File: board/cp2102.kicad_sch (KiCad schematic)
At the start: 7 parts, among them U1 CP2102N-Axx-xQFN28

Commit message: finished layout
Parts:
- C1, C2: footprint (none) -> Capacitor_SMD:C_0603_1608Metric
- R1, R2, R3, R6: footprint (none) -> Resistor_SMD:R_0603_1608Metric
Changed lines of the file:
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@@
       (effects (font (size 1.27 1.27)) (justify left))
     )
-    (property "Footprint" "" (at 125.73 86.36 0)
+    (property "Footprint" "Capacitor_SMD:C_0603_1608Metric" (at 125.73 86.36 0)
       (effects (font (size 1.27 1.27)) hide)
     )
@@
       (effects (font (size 1.27 1.27)) (justify left))
     )
-    (property "Footprint" "" (at 139.7 60.325 0)
+    (property "Footprint" "Resistor_SMD:R_0603_1608Metric" (at 139.7 60.325 0)
       (effects (font (size 1.27 1.27)) hide)
     )
@@
       (effects (font (size 1.27 1.27)))
     )
-    (property "Footprint" "" (at 175.26 94.615 0)
+    (property "Footprint" "Resistor_SMD:R_0603_1608Metric" (at 175.26 94.615 0)
       (effects (font (size 1.27 1.27)) hide)
     )
@@
       (effects (font (size 1.27 1.27)) (justify left))
     )
-    (property "Footprint" "" (at 163.83 57.785 0)
+    (property "Footprint" "Capacitor_SMD:C_0603_1608Metric" (at 163.83 57.785 0)
       (effects (font (size 1.27 1.27)) hide)
     )
@@
       (effects (font (size 1.27 1.27)) (justify left))
     )
-    (property "Footprint" "" (at 116.205 77.47 0)
+    (property "Footprint" "Resistor_SMD:R_0603_1608Metric" (at 116.205 77.47 0)
       (effects (font (size 1.27 1.27)) hide)
     )
@@
       (effects (font (size 1.27 1.27)) (justify left))
     )
-    (property "Footprint" "" (at 116.205 86.36 0)
+    (property "Footprint" "Resistor_SMD:R_0603_1608Metric" (at 116.205 86.36 0)
       (effects (font (size 1.27 1.27)) hide)
     )

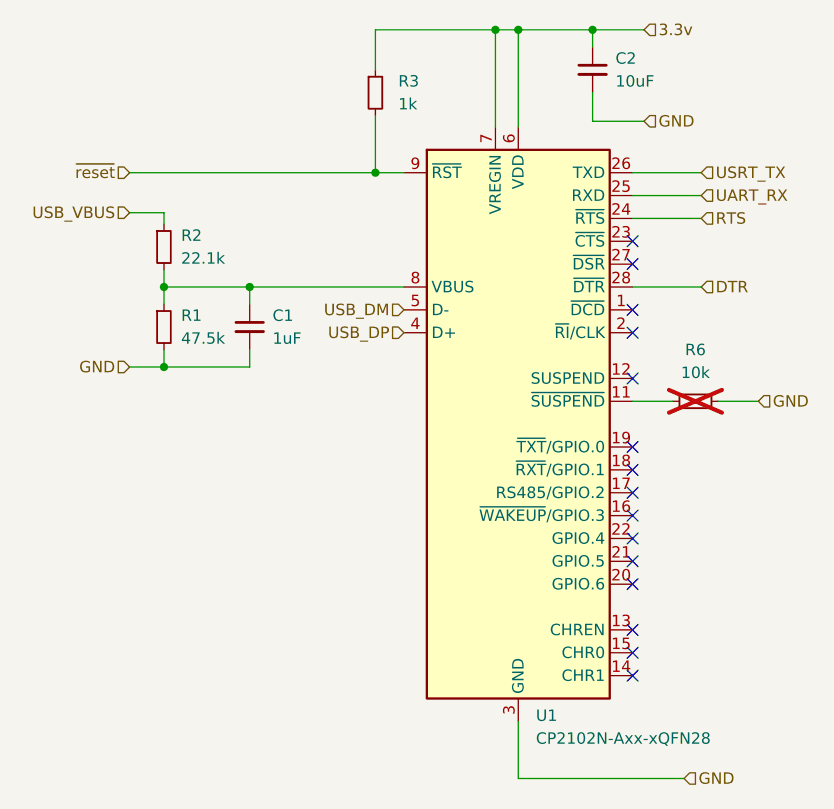
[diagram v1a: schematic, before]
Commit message: added lcsc numbers
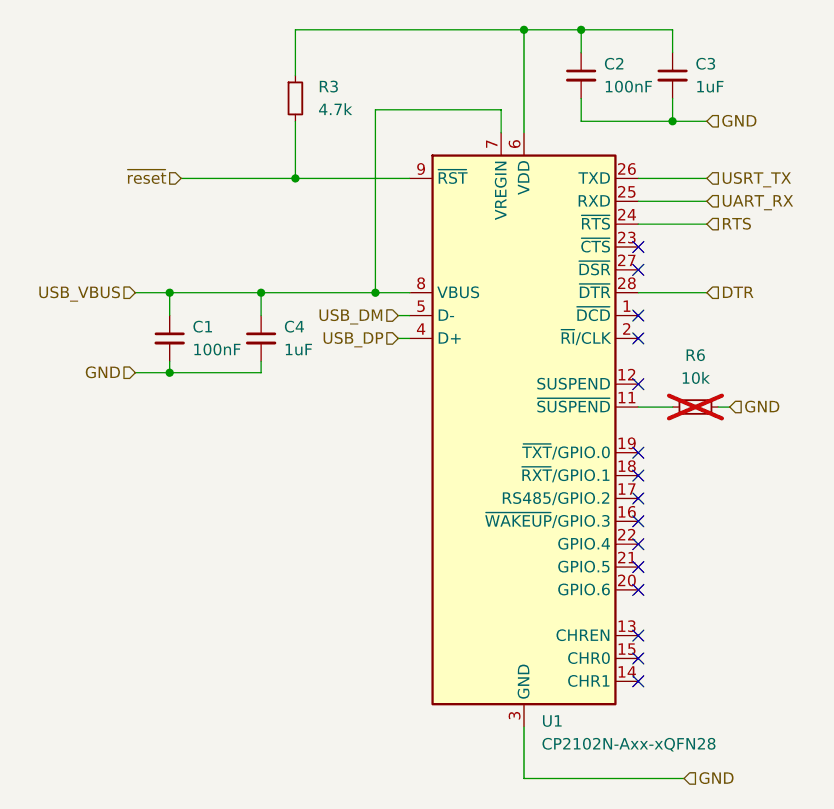
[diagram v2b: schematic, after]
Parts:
- removed R1: 47.5k, Resistor_SMD:R_0603_1608Metric, symbol Device:R_Small
- removed R2: 22.1k, Resistor_SMD:R_0603_1608Metric, symbol Device:R_Small
- added C3, C4: 1uF, Capacitor_SMD:C_0402_1005Metric, symbol Device:C_Small
- C1: value 1uF -> 100nF; footprint Capacitor_SMD:C_0603_1608Metric -> Capacitor_SMD:C_0402_1005Metric; lcsc (none) -> C1525
- C2: value 10uF -> 100nF; footprint Capacitor_SMD:C_0603_1608Metric -> Capacitor_SMD:C_0402_1005Metric; lcsc (none) -> C1525
- R3: value 1k -> 4.7k; footprint Resistor_SMD:R_0603_1608Metric -> Resistor_SMD:R_0402_1005Metric; lcsc (none) -> C25900
- R6: footprint Resistor_SMD:R_0603_1608Metric -> Resistor_SMD:R_0402_1005Metric; lcsc (none) -> C25744
- U1: lcsc (none) -> C964632
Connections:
- net GND: now also C3.2, C4.2
- net USB_VBUS: now also C1.1, U1.7 (VREGIN), U1.8 (VBUS), C4.1
- net 3.3v: no longer names the net of C2.1, R3.1, U1.6 (VDD)
- net 3.3v: now also C3.1; no longer U1.7 (VREGIN)
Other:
- moved on the sheet: C2, R3, R6, U1
